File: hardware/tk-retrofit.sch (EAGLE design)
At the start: 37 parts, among them U2 DRDC3105, U7 MIC5233, U8 NRF52832, Y1 32MHz, Y2 32.768kHz

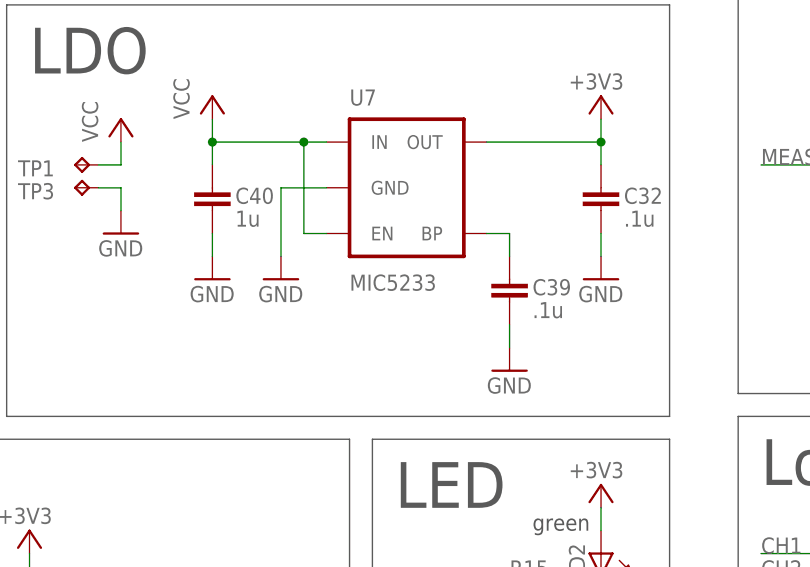
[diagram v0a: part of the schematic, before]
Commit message: tk-retrofit: fix ldo p/n
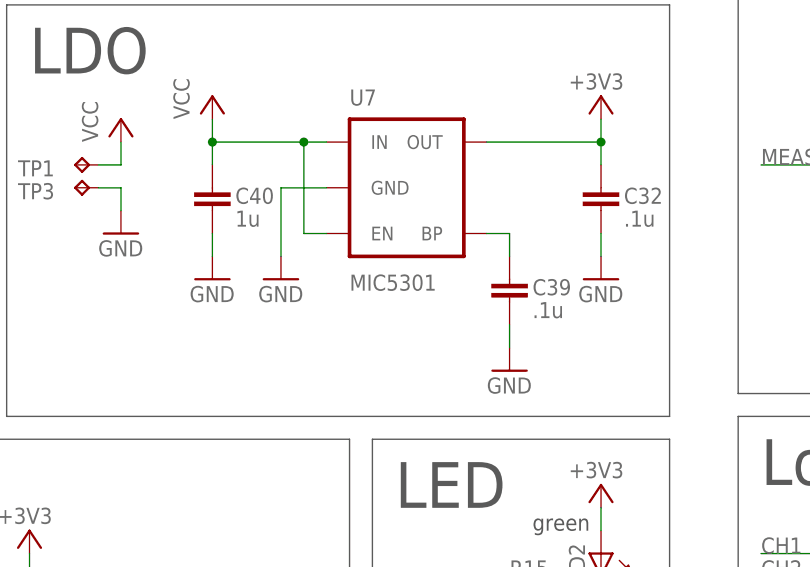
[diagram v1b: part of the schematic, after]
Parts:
- U7: value MIC5233 -> MIC5301
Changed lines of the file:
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@@
 <grid distance="0.1" unitdist="inch" unit="inch" style="lines" multiple="1" display="no" altdistance="0.01" altunitdist="inch" altunit="inch"/>
 <layers>
-<layer number="1" name="Top" color="4" fill="1" visible="yes" active="no"/>
-<layer number="16" name="Bottom" color="1" fill="1" visible="yes" active="no"/>
-<layer number="17" name="Pads" color="2" fill="1" visible="yes" active="no"/>
-<layer number="18" name="Vias" color="2" fill="1" visible="yes" active="no"/>
-<layer number="19" name="Unrouted" color="6" fill="1" visible="yes" active="no"/>
-<layer number="20" name="Dimension" color="24" fill="1" visible="yes" active="no"/>
-<layer number="21" name="tPlace" color="7" fill="1" visible="yes" active="no"/>
-<layer number="22" name="bPlace" color="7" fill="1" visible="yes" active="no"/>
-<layer number="23" name="tOrigins" color="15" fill="1" visible="yes" active="no"/>
-<layer number="24" name="bOrigins" color="15" fill="1" visible="yes" active="no"/>
-<layer number="25" name="tNames" color="7" fill="1" visible="yes" active="no"/>
-<layer number="26" name="bNames" color="7" fill="1" visible="yes" active="no"/>
-<layer number="27" name="tValues" color="7" fill="1" visible="yes" active="no"/>
-<layer number="28" name="bValues" color="7" fill="1" visible="yes" active="no"/>
+<layer number="1" name="Top" color="4" fill="1" visible="no" active="no"/>
+<layer number="16" name="Bottom" color="1" fill="1" visible="no" active="no"/>
+<layer number="17" name="Pads" color="2" fill="1" visible="no" active="no"/>
+<layer number="18" name="Vias" color="2" fill="1" visible="no" active="no"/>
+<layer number="19" name="Unrouted" color="6" fill="1" visible="no" active="no"/>
+<layer number="20" name="Dimension" color="24" fill="1" visible="no" active="no"/>
+<layer number="21" name="tPlace" color="7" fill="1" visible="no" active="no"/>
+<layer number="22" name="bPlace" color="7" fill="1" visible="no" active="no"/>
+<layer number="23" name="tOrigins" color="15" fill="1" visible="no" active="no"/>
+<layer number="24" name="bOrigins" color="15" fill="1" visible="no" active="no"/>
+<layer number="25" name="tNames" color="7" fill="1" visible="no" active="no"/>
+<layer number="26" name="bNames" color="7" fill="1" visible="no" active="no"/>
+<layer number="27" name="tValues" color="7" fill="1" visible="no" active="no"/>
+<layer number="28" name="bValues" color="7" fill="1" visible="no" active="no"/>
 <layer number="29" name="tStop" color="7" fill="3" visible="no" active="no"/>
 <layer number="30" name="bStop" color="7" fill="6" visible="no" active="no"/>
@@
 <layer number="35" name="tGlue" color="7" fill="4" visible="no" active="no"/>
 <layer number="36" name="bGlue" color="7" fill="5" visible="no" active="no"/>
-<layer number="37" name="tTest" color="7" fill="1" visible="yes" active="no"/>
-<layer number="38" name="bTest" color="7" fill="1" visible="yes" active="no"/>
+<layer number="37" name="tTest" color="7" fill="1" visible="no" active="no"/>
+<layer number="38" name="bTest" color="7" fill="1" visible="no" active="no"/>
 <layer number="39" name="tKeepout" color="4" fill="11" visible="no" active="no"/>
 <layer number="40" name="bKeepout" color="1" fill="11" visible="no" active="no"/>
@@
 <layer number="44" name="Drills" color="7" fill="1" visible="no" active="no"/>
 <layer number="45" name="Holes" color="7" fill="1" visible="no" active="no"/>
-<layer number="46" name="Milling" color="3" fill="1" visible="yes" active="no"/>
-<layer number="47" name="Measures" color="7" fill="1" visible="yes" active="no"/>
-<layer number="48" name="Document" color="7" fill="1" visible="yes" active="no"/>
-<layer number="49" name="Reference" color="7" fill="1" visible="yes" active="no"/>
-<layer number="50" name="dxf" color="7" fill="1" visible="yes" active="no"/>
-<layer number="51" name="tDocu" color="7" fill="1" visible="yes" active="no"/>
-<layer number="52" name="bDocu" color="7" fill="1" visible="yes" active="no"/>
-<layer number="53" name="tGND_GNDA" color="7" fill="9" visible="yes" active="no"/>
-<layer number="54" name="bGND_GNDA" color="1" fill="9" visible="yes" active="no"/>
-<layer number="56" name="wert" color="7" fill="1" visible="yes" active="no"/>
-<layer number="57" name="tCAD" color="7" fill="1" visible="yes" active="no"/>
-<layer number="59" name="tCarbon" color="7" fill="1" visible="yes" active="no"/>
-<layer number="60" name="bCarbon" color="7" fill="1" visible="yes" active="no"/>
+<layer number="46" name="Milling" color="3" fill="1" visible="no" active="no"/>
+<layer number="47" name="Measures" color="7" fill="1" visible="no" active="no"/>
+<layer number="48" name="Document" color="7" fill="1" visible="no" active="no"/>
+<layer number="49" name="Reference" color="7" fill="1" visible="no" active="no"/>
+<layer number="50" name="dxf" color="7" fill="1" visible="no" active="no"/>
+<layer number="51" name="tDocu" color="7" fill="1" visible="no" active="no"/>
+<layer number="52" name="bDocu" color="7" fill="1" visible="no" active="no"/>
+<layer number="53" name="tGND_GNDA" color="7" fill="9" visible="no" active="no"/>
+<layer number="54" name="bGND_GNDA" color="1" fill="9" visible="no" active="no"/>
+<layer number="56" name="wert" color="7" fill="1" visible="no" active="no"/>
+<layer number="57" name="tCAD" color="7" fill="1" visible="no" active="no"/>
+<layer number="59" name="tCarbon" color="7" fill="1" visible="no" active="no"/>
+<layer number="60" name="bCarbon" color="7" fill="1" visible="no" active="no"/>
 <layer number="88" name="SimResults" color="9" fill="1" visible="yes" active="yes"/>
 <layer number="89" name="SimProbes" color="9" fill="1" visible="yes" active="yes"/>
@@
 <part name="C32" library="balto" deviceset="C" device="0603" value=".1u"/>
 <part name="GND41" library="supply1" deviceset="GND" device=""/>
-<part name="U7" library="SparkFun-PowerIC" deviceset="V_REG_LDO" device="SMD" value="MIC5233"/>
+<part name="U7" library="SparkFun-PowerIC" deviceset="V_REG_LDO" device="SMD" value="MIC5301"/>
 <part name="GND42" library="supply1" deviceset="GND" device=""/>
 <part name="C39" library="balto" deviceset="C" device="0603" value=".1u"/>

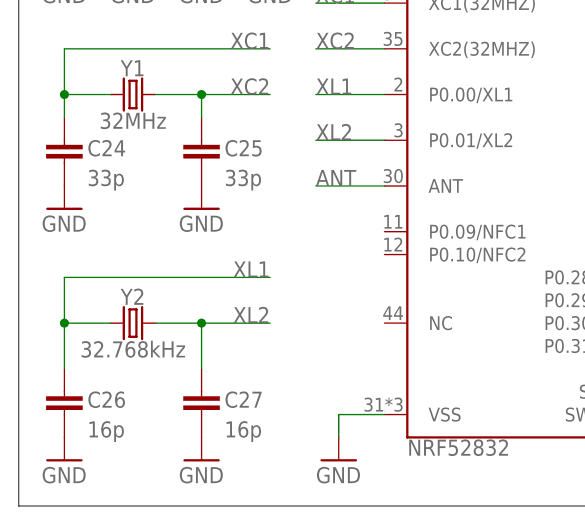
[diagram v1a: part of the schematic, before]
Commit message: hw: tk-retrofit: change xtal cap values
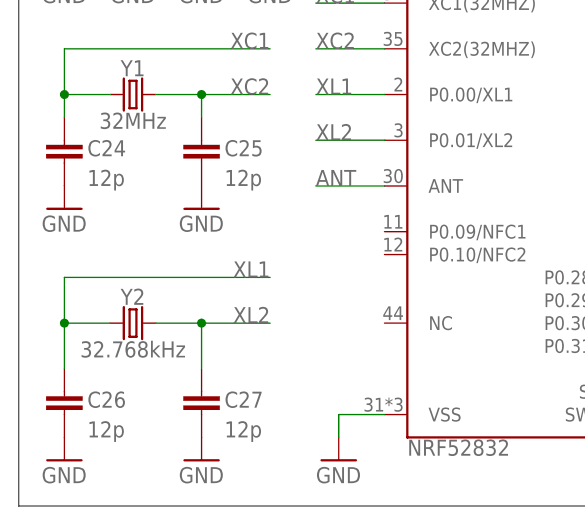
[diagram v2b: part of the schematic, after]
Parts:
- C24, C25: value 33p -> 12p
- C26, C27: value 16p -> 12p
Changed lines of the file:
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@@
 <part name="Y1" library="SparkFun-Clocks" deviceset="CRYSTAL" device="SMD-3.2X2.5" value="32MHz"/>
 <part name="Y2" library="SparkFun-Clocks" deviceset="CRYSTAL-32.768KHZ" device="SMD-3.2X1.5" value="32.768kHz"/>
-<part name="C24" library="balto" deviceset="C" device="0603" value="33p"/>
-<part name="C25" library="balto" deviceset="C" device="0603" value="33p"/>
-<part name="C26" library="balto" deviceset="C" device="0603" value="16p"/>
-<part name="C27" library="balto" deviceset="C" device="0603" value="16p"/>
+<part name="C24" library="balto" deviceset="C" device="0603" value="12p"/>
+<part name="C25" library="balto" deviceset="C" device="0603" value="12p"/>
+<part name="C26" library="balto" deviceset="C" device="0603" value="12p"/>
+<part name="C27" library="balto" deviceset="C" device="0603" value="12p"/>
 <part name="C28" library="balto" deviceset="C" device="0603" value="dnp"/>
 <part name="GND23" library="supply1" deviceset="GND" device=""/>
